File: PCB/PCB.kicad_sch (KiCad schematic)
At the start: 111 parts, among them J1 USB_B_Micro, J2 Conn_01x02, Q1 PJA3428, Q2 PJA3428, Q3 AO3401A, SW1 SW_Push, SW2 SW_Push, SW3 SW_Push, SW4 ON/OFF, U1 ESP32-PICO-MINI-02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

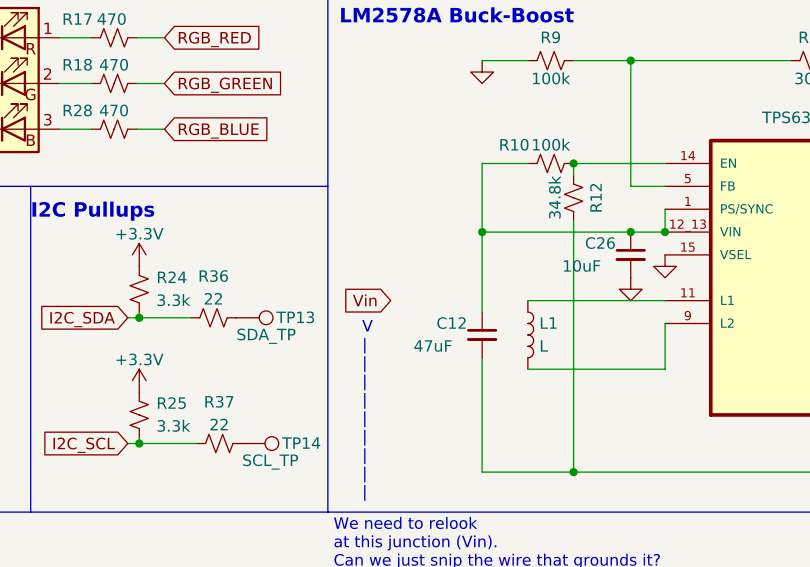
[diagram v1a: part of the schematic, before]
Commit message: buck-boost edits
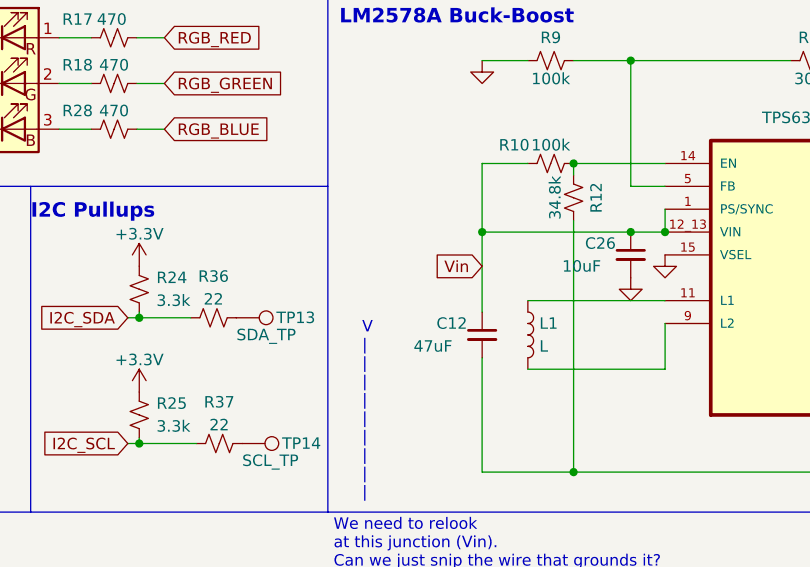
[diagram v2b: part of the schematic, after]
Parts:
- L1: footprint Inductor_SMD:L_0805_2012Metric_Pad1.15x1.40mm_HandSolder -> inductor:IHLP1212BZERR56M11
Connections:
- net Vin: now also C12.1, C26.1, R10.1, U4.1 (PS/SYNC), U4.12_13 (VIN)
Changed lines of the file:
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@@
     )
   )
-  (global_label "Vin" (shape input) (at 295.91 124.46 180) (fields_autoplaced)
+  (global_label "Vin" (shape input) (at 306.07 120.65 180) (fields_autoplaced)
     (effects (font (size 1.27 1.27)) (justify right))
-    (property "Intersheet References" "${INTERSHEET_REFS}" (id 0) (at 290.6545 124.3806 0)
+    (property "Intersheet References" "${INTERSHEET_REFS}" (id 0) (at 300.8145 120.5706 0)
       (effects (font (size 1.27 1.27)) (justify right) hide)
     )
@@
       (effects (font (size 1.27 1.27)) (justify left))
     )
-    (property "Footprint" "Inductor_SMD:L_0805_2012Metric_Pad1.15x1.40mm_HandSolder" (id 2) (at 311.15 128.27 0)
+    (property "Footprint" "inductor:IHLP1212BZERR56M11" (id 2) (at 311.15 128.27 0)
       (effects (font (size 1.27 1.27)) hide)
     )
@@
     )
     (path "/c386aa6a-54a9-4a0e-9ad5-3e2e9aeae025"
-      (reference "L1") (unit 1) (value "L") (footprint "Inductor_SMD:L_0805_2012Metric_Pad1.15x1.40mm_HandSolder")
+      (reference "L1") (unit 1) (value "L") (footprint "inductor:IHLP1212BZERR56M11")
     )
     (path "/cef27ab4-b73f-410e-8967-9f4b41c610a5"

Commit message: buck-boost routing 1
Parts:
- C12: footprint Capacitor_SMD:C_0603_1608Metric -> Capacitor_SMD:C_1206_3216Metric_Pad1.33x1.80mm_HandSolder
- C13: footprint Capacitor_SMD:C_0603_1608Metric -> Capacitor_SMD:C_0402_1005Metric_Pad0.74x0.62mm_HandSolder
- C14: footprint Capacitor_SMD:C_0603_1608Metric -> Capacitor_SMD:C_0201_0603Metric
- C17: footprint Capacitor_SMD:C_0603_1608Metric -> Capacitor_SMD:C_1206_3216Metric
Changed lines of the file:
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@@
       (effects (font (size 1.27 1.27)) (justify left))
     )
-    (property "Footprint" "Capacitor_SMD:C_0603_1608Metric" (id 2) (at 367.03 125.73 0)
+    (property "Footprint" "Capacitor_SMD:C_0402_1005Metric_Pad0.74x0.62mm_HandSolder" (id 2) (at 367.03 125.73 0)
       (effects (font (size 1.27 1.27)) hide)
     )
@@
       (effects (font (size 1.27 1.27)) (justify left))
     )
-    (property "Footprint" "Capacitor_SMD:C_0603_1608Metric" (id 2) (at 389.89 124.46 0)
+    (property "Footprint" "Capacitor_SMD:C_0201_0603Metric" (id 2) (at 389.89 124.46 0)
       (effects (font (size 1.27 1.27)) hide)
     )
@@
       (effects (font (size 1.27 1.27)) (justify left))
     )
-    (property "Footprint" "Capacitor_SMD:C_0603_1608Metric" (id 2) (at 306.07 128.27 0)
+    (property "Footprint" "Capacitor_SMD:C_1206_3216Metric_Pad1.33x1.80mm_HandSolder" (id 2) (at 306.07 128.27 0)
       (effects (font (size 1.27 1.27)) hide)
     )
@@
       (effects (font (size 1.27 1.27)) (justify left))
     )
-    (property "Footprint" "Capacitor_SMD:C_0603_1608Metric" (id 2) (at 397.51 124.46 0)
+    (property "Footprint" "Capacitor_SMD:C_1206_3216Metric" (id 2) (at 397.51 124.46 0)
       (effects (font (size 1.27 1.27)) hide)
     )
@@
     )
     (path "/395ec407-9028-49e9-8808-58f5d58d2657"
-      (reference "C12") (unit 1) (value "47uF") (footprint "Capacitor_SMD:C_0603_1608Metric")
+      (reference "C12") (unit 1) (value "47uF") (footprint "Capacitor_SMD:C_1206_3216Metric_Pad1.33x1.80mm_HandSolder")
     )
     (path "/1064231c-bfd3-489f-ae80-b5249537604d"
-      (reference "C13") (unit 1) (value "10uF") (footprint "Capacitor_SMD:C_0603_1608Metric")
+      (reference "C13") (unit 1) (value "10uF") (footprint "Capacitor_SMD:C_0402_1005Metric_Pad0.74x0.62mm_HandSolder")
     )
     (path "/1efd981a-b294-4f8f-8a3b-cd723ec3f3c5"
-      (reference "C14") (unit 1) (value "10uF") (footprint "Capacitor_SMD:C_0603_1608Metric")
+      (reference "C14") (unit 1) (value "10uF") (footprint "Capacitor_SMD:C_0201_0603Metric")
     )
     (path "/5cf5aff0-dc8a-4f55-b7fe-2729fa1be8c6"
@@
     )
     (path "/62c4ea4f-a8d4-412b-b281-d9bb9978b21a"
-      (reference "C17") (unit 1) (value "47uF") (footprint "Capacitor_SMD:C_0603_1608Metric")
+      (reference "C17") (unit 1) (value "47uF") (footprint "Capacitor_SMD:C_1206_3216Metric")
     )
     (path "/d95f2a14-12b0-408b-b3aa-ddfd14eabcf1"

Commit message: buck/boost
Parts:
- C13: footprint Capacitor_SMD:C_0402_1005Metric_Pad0.74x0.62mm_HandSolder -> Capacitor_SMD:C_0603_1608Metric
- C14: footprint Capacitor_SMD:C_0201_0603Metric -> Capacitor_SMD:C_0603_1608Metric
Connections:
- net +3.3V: now also C14.1, C17.1, C27.1, R13.1, R14.1, U4.7_8 (VOUT)
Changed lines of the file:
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@@
   (junction (at 326.39 116.84) (diameter 0) (color 0 0 0 0)
   )
+  (junction (at 397.51 121.92) (diameter 0) (color 0 0 0 0)
+  )
   (junction (at 375.285 33.02) (diameter 0) (color 0 0 0 0)
   )
@@
       (effects (font (size 1.27 1.27)) (justify left))
     )
-    (property "Footprint" "Capacitor_SMD:C_0402_1005Metric_Pad0.74x0.62mm_HandSolder" (id 2) (at 367.03 125.73 0)
+    (property "Footprint" "Capacitor_SMD:C_0603_1608Metric" (id 2) (at 367.03 125.73 0)
       (effects (font (size 1.27 1.27)) hide)
     )
@@
       (effects (font (size 1.27 1.27)) (justify left))
     )
-    (property "Footprint" "Capacitor_SMD:C_0201_0603Metric" (id 2) (at 389.89 124.46 0)
+    (property "Footprint" "Capacitor_SMD:C_0603_1608Metric" (id 2) (at 389.89 124.46 0)
       (effects (font (size 1.27 1.27)) hide)
     )
@@
     (pin "2")
   )
+  (symbol (lib_id "power:+3.3V") (at 397.51 121.92 0) (unit 1)
+    (in_bom yes) (on_board yes)
+    (property "Reference" "#PWR?" (id 0) (at 397.51 125.73 0)
+      (effects (font (size 1.27 1.27)) hide)
+    )
+    (property "Value" "+3.3V" (id 1) (at 397.51 118.11 0))
+    (property "Footprint" "" (id 2) (at 397.51 121.92 0)
+      (effects (font (size 1.27 1.27)) hide)
+    )
+    (property "Datasheet" "" (id 3) (at 397.51 121.92 0)
+      (effects (font (size 1.27 1.27)) hide)
+    )
+    (pin "1")
+  )
   (symbol (lib_id "power:+3.3V") (at 16.51 67.945 0) (unit 1)
     (in_bom yes) (on_board yes) (fields_autoplaced)
@@
       (reference "#PWR0133") (unit 1) (value "GND") (footprint "")
     )
+    (path "/f9a82e16-6e31-40b7-8380-a1ae7b429d70"
+      (reference "#PWR?") (unit 1) (value "+3.3V") (footprint "")
+    )
     (path "/52cf2d49-7911-4779-ac42-2bcd30f30395"
       (reference "C1") (unit 1) (value "10uF") (footprint "Capacitor_SMD:C_0603_1608Metric")
@@
     )
     (path "/1064231c-bfd3-489f-ae80-b5249537604d"
-      (reference "C13") (unit 1) (value "10uF") (footprint "Capacitor_SMD:C_0402_1005Metric_Pad0.74x0.62mm_HandSolder")
+      (reference "C13") (unit 1) (value "10uF") (footprint "Capacitor_SMD:C_0603_1608Metric")
     )
     (path "/1efd981a-b294-4f8f-8a3b-cd723ec3f3c5"
-      (reference "C14") (unit 1) (value "10uF") (footprint "Capacitor_SMD:C_0201_0603Metric")
+      (reference "C14") (unit 1) (value "10uF") (footprint "Capacitor_SMD:C_0603_1608Metric")
     )
     (path "/5cf5aff0-dc8a-4f55-b7fe-2729fa1be8c6"

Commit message: buck/boost more progress
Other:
- note added: "TPS63070 Buck-Boost"
- note removed: "LM2578A Buck-Boost"
- note removed: "V | | | | | | | | |"
- note removed: "We need to relook at this junction (Vin). Can we just snip the wire that grounds it?"
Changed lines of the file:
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@@
     (effects (font (size 1.6 1.6) (thickness 0.32) bold) (justify left bottom))
-  )
-  (text "We need to relook \nat this junction (Vin).\nCan we just snip the wire that grounds it?"
-    (at 289.56 154.305 0)
-    (effects (font (size 1.27 1.27)) (justify left bottom))
   )
   (text "ESP32\n" (at 13.335 60.325 0)
@@
     (effects (font (size 1.27 1.27) bold) (justify left bottom))
   )
-  (text "V\n|\n|\n|\n|\n|\n|\n|\n|\n|" (at 292.735 146.685 0)
-    (effects (font (size 1.27 1.27)) (justify left bottom))
-  )
   (text "ESP32 Auto-Program Transistors" (at 13.335 151.765 0)
     (effects (font (size 1.6 1.6) (thickness 0.32) bold) (justify left bottom))
@@
     (effects (font (size 1.6 1.6) (thickness 0.32) bold) (justify left bottom))
   )
-  (text "LM2578A Buck-Boost" (at 290.195 93.98 0)
+  (text "TPS63070 Buck-Boost" (at 288.925 92.075 0)
     (effects (font (size 1.6 1.6) (thickness 0.32) bold) (justify left bottom))
   )

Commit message: button update
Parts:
- removed TP1: TDI, TestPoint:TestPoint_Pad_D1.0mm, symbol Connector:TestPoint
- removed TP10: TDO, TestPoint:TestPoint_Pad_D1.0mm, symbol Connector:TestPoint
- removed TP2: TCK, TestPoint:TestPoint_Pad_D1.0mm, symbol Connector:TestPoint
- removed TP9: TMS, TestPoint:TestPoint_Pad_D1.0mm, symbol Connector:TestPoint
- added C28: 100nF, Capacitor_SMD:C_0603_1608Metric, symbol Device:C_Small
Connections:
- net GND: now also C28.2
- net SESSION_BUTTON: now also C28.1
- no-connect marks 12 -> 16
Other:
- moved on the sheet: R24, R25, R36, R37, R39, R40, R41, R42, TP13, TP14

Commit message: final changes
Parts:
- D2: value 1N4148 -> B5819W
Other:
- moved on the sheet: C28, R21, SW3
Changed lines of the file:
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@@
   (junction (at 321.945 60.96) (diameter 0) (color 0 0 0 0)
   )
-  (junction (at 245.745 129.54) (diameter 0) (color 0 0 0 0)
+  (junction (at 253.365 128.905) (diameter 0) (color 0 0 0 0)
   )
   (junction (at 389.89 143.51) (diameter 0) (color 0 0 0 0)
@@
     (stroke (width 0) (type default) (color 0 0 0 0))
   )
-  (wire (pts (xy 245.745 129.54) (xy 245.745 130.81))
+  (wire (pts (xy 253.365 128.905) (xy 253.365 130.175))
     (stroke (width 0) (type default) (color 0 0 0 0))
   )
@@
     (stroke (width 0) (type default) (color 0 0 0 0))
   )
-  (wire (pts (xy 254.635 133.35) (xy 254.635 129.54))
+  (wire (pts (xy 262.255 132.715) (xy 262.255 128.905))
     (stroke (width 0) (type default) (color 0 0 0 0))
   )
@@
     (stroke (width 0) (type default) (color 0 0 0 0))
   )
-  (wire (pts (xy 245.745 128.905) (xy 245.745 129.54))
+  (wire (pts (xy 253.365 128.27) (xy 253.365 128.905))
     (stroke (width 0) (type default) (color 0 0 0 0))
   )
@@
     (stroke (width 0) (type default) (color 0 0 0 0))
   )
-  (wire (pts (xy 245.11 129.54) (xy 245.745 129.54))
+  (wire (pts (xy 252.73 128.905) (xy 253.365 128.905))
     (stroke (width 0) (type default) (color 0 0 0 0))
   )
@@
     (stroke (width 0) (type default) (color 0 0 0 0))
   )
-  (wire (pts (xy 254.635 129.54) (xy 245.745 129.54))
+  (wire (pts (xy 262.255 128.905) (xy 253.365 128.905))
     (stroke (width 0) (type default) (color 0 0 0 0))
   )
@@
     )
   )
-  (global_label "SESSION_BUTTON" (shape input) (at 245.11 129.54 180) (fields_autoplaced)
+  (global_label "SESSION_BUTTON" (shape input) (at 252.73 128.905 180) (fields_autoplaced)
     (effects (font (size 1.27 1.27)) (justify right))
-    (property "Intersheet References" "${INTERSHEET_REFS}" (id 0) (at 226.4893 129.4606 0)
+    (property "Intersheet References" "${INTERSHEET_REFS}" (id 0) (at 234.1093 128.8256 0)
       (effects (font (size 1.27 1.27)) (justify right) hide)
     )
@@
     (pin "1")
   )
-  (symbol (lib_id "power:GND") (at 245.745 140.97 0) (unit 1)
+  (symbol (lib_id "power:GND") (at 253.365 140.335 0) (unit 1)
     (in_bom yes) (on_board yes)
-    (property "Reference" "#PWR0123" (id 0) (at 245.745 147.32 0)
+    (property "Reference" "#PWR0123" (id 0) (at 253.365 146.685 0)
       (effects (font (size 1.27 1.27)) hide)
     )
-    (property "Value" "GND" (id 1) (at 250.825 144.78 0)
+    (property "Value" "GND" (id 1) (at 258.445 144.145 0)
       (effects (font (size 1.27 1.27)) hide)
     )
-    (property "Footprint" "" (id 2) (at 245.745 140.97 0)
+    (property "Footprint" "" (id 2) (at 253.365 140.335 0)
       (effects (font (size 1.27 1.27)) hide)
     )
-    (property "Datasheet" "" (id 3) (at 245.745 140.97 0)
+    (property "Datasheet" "" (id 3) (at 253.365 140.335 0)
       (effects (font (size 1.27 1.27)) hide)
     )
@@
     (pin "1")
   )
-  (symbol (lib_id "Switch:SW_Push") (at 245.745 135.89 270) (unit 1)
+  (symbol (lib_id "Switch:SW_Push") (at 253.365 135.255 270) (unit 1)
     (in_bom yes) (on_board yes)
-    (property "Reference" "SW3" (id 0) (at 244.475 135.255 90)
+    (property "Reference" "SW3" (id 0) (at 252.095 134.62 90)
       (effects (font (size 1.27 1.27)) (justify right))
     )
-    (property "Value" "SW_Push" (id 1) (at 244.475 137.16 90)
+    (property "Value" "SW_Push" (id 1) (at 252.095 136.525 90)
       (effects (font (size 1.27 1.27)) (justify right))
     )
-    (property "Footprint" "Button_Switch_THT:SW_Tactile_SPST_Angled_PTS645Vx58-2LFS" (id 2) (at 250.825 135.89 0)
+    (property "Footprint" "Button_Switch_THT:SW_Tactile_SPST_Angled_PTS645Vx58-2LFS" (id 2) (at 258.445 135.255 0)
       (effects (font (size 1.27 1.27)) hide)
     )
-    (property "Datasheet" "~" (id 3) (at 250.825 135.89 0)
+    (property "Datasheet" "~" (id 3) (at 258.445 135.255 0)
       (effects (font (size 1.27 1.27)) hide)
     )
@@
     (pin "2")
   )
-  (symbol (lib_id "power:GND") (at 254.635 138.43 0) (unit 1)
+  (symbol (lib_id "power:GND") (at 262.255 137.795 0) (unit 1)
     (in_bom yes) (on_board yes)
-    (property "Reference" "#PWR0135" (id 0) (at 254.635 144.78 0)
+    (property "Reference" "#PWR0135" (id 0) (at 262.255 144.145 0)
       (effects (font (size 1.27 1.27)) hide)
     )
-    (property "Value" "GND" (id 1) (at 259.715 142.24 0)
+    (property "Value" "GND" (id 1) (at 267.335 141.605 0)
       (effects (font (size 1.27 1.27)) hide)
     )
-    (property "Footprint" "" (id 2) (at 254.635 138.43 0)
+    (property "Footprint" "" (id 2) (at 262.255 137.795 0)
       (effects (font (size 1.27 1.27)) hide)
     )
-    (property "Datasheet" "" (id 3) (at 254.635 138.43 0)
+    (property "Datasheet" "" (id 3) (at 262.255 137.795 0)
       (effects (font (size 1.27 1.27)) hide)
     )
@@
   (symbol (lib_id "Diode:1N4148") (at 125.73 30.48 90) (unit 1)
     (in_bom yes) (on_board yes) (fields_autoplaced)
-    (property "Reference" "D2" (id 0) (at 127.762 29.6453 90)
+    (property "Reference" "D2" (id 0) (at 128.27 29.2099 90)
       (effects (font (size 1.27 1.27)) (justify right))
     )
-    (property "Value" "1N4148" (id 1) (at 127.762 32.1822 90)
+    (property "Value" "B5819W" (id 1) (at 128.27 31.7499 90)
       (effects (font (size 1.27 1.27)) (justify right))
     )
@@
     (pin "2")
   )
-  (symbol (lib_id "power:+3.3V") (at 245.745 123.825 0) (unit 1)
+  (symbol (lib_id "power:+3.3V") (at 253.365 123.19 0) (unit 1)
     (in_bom yes) (on_board yes) (fields_autoplaced)
-    (property "Reference" "#PWR0124" (id 0) (at 245.745 127.635 0)
+    (property "Reference" "#PWR0124" (id 0) (at 253.365 127 0)
       (effects (font (size 1.27 1.27)) hide)
     )
-    (property "Value" "+3.3V" (id 1) (at 245.745 120.2492 0))
-    (property "Footprint" "" (id 2) (at 245.745 123.825 0)
+    (property "Value" "+3.3V" (id 1) (at 253.365 119.6142 0))
+    (property "Footprint" "" (id 2) (at 253.365 123.19 0)
       (effects (font (size 1.27 1.27)) hide)
     )
-    (property "Datasheet" "" (id 3) (at 245.745 123.825 0)
+    (property "Datasheet" "" (id 3) (at 253.365 123.19 0)
       (effects (font (size 1.27 1.27)) hide)
     )
@@
     (pin "3")
   )
-  (symbol (lib_id "Device:R_Small_US") (at 245.745 126.365 0) (unit 1)
+  (symbol (lib_id "Device:R_Small_US") (at 253.365 125.73 0) (unit 1)
     (in_bom yes) (on_board yes) (fields_autoplaced)
-    (property "Reference" "R21" (id 0) (at 248.285 125.0949 0)
+    (property "Reference" "R21" (id 0) (at 255.905 124.4599 0)
       (effects (font (size 1.27 1.27)) (justify left))
     )
-    (property "Value" "10k" (id 1) (at 248.285 127.6349 0)
+    (property "Value" "10k" (id 1) (at 255.905 126.9999 0)
       (effects (font (size 1.27 1.27)) (justify left))
     )
-    (property "Footprint" "Resistor_SMD:R_0603_1608Metric" (id 2) (at 245.745 126.365 0)
+    (property "Footprint" "Resistor_SMD:R_0603_1608Metric" (id 2) (at 253.365 125.73 0)
       (effects (font (size 1.27 1.27)) hide)
     )
-    (property "Datasheet" "~" (id 3) (at 245.745 126.365 0)
+    (property "Datasheet" "~" (id 3) (at 253.365 125.73 0)
       (effects (font (size 1.27 1.27)) hide)
     )
@@
     (pin "1")
   )
-  (symbol (lib_id "Device:C_Small") (at 254.635 135.89 0) (unit 1)
+  (symbol (lib_id "Device:C_Small") (at 262.255 135.255 0) (unit 1)
     (in_bom yes) (on_board yes) (fields_autoplaced)
-    (property "Reference" "C28" (id 0) (at 257.175 134.6262 0)
+    (property "Reference" "C28" (id 0) (at 264.795 133.9912 0)
       (effects (font (size 1.27 1.27)) (justify left))
     )
-    (property "Value" "100nF" (id 1) (at 257.175 137.1662 0)
+    (property "Value" "100nF" (id 1) (at 264.795 136.5312 0)
       (effects (font (size 1.27 1.27)) (justify left))
     )
-    (property "Footprint" "Capacitor_SMD:C_0603_1608Metric" (id 2) (at 254.635 135.89 0)
+    (property "Footprint" "Capacitor_SMD:C_0603_1608Metric" (id 2) (at 262.255 135.255 0)
       (effects (font (size 1.27 1.27)) hide)
     )
-    (property "Datasheet" "~" (id 3) (at 254.635 135.89 0)
+    (property "Datasheet" "~" (id 3) (at 262.255 135.255 0)
       (effects (font (size 1.27 1.27)) hide)
     )
@@
     )
     (path "/581ca598-1d01-4057-bec3-5cf6c2d6dd7c"
-      (reference "D2") (unit 1) (value "1N4148") (footprint "Diode_SMD:D_1206_3216Metric")
+      (reference "D2") (unit 1) (value "B5819W") (footprint "Diode_SMD:D_1206_3216Metric")
     )
     (path "/0468a543-7392-406e-a1e2-1b00bf8a5b37"

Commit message: schem edits
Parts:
- C13: value 10uF -> 100 nF
- C27: value 100nF -> 10uF
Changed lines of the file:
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@@
       (effects (font (size 1.27 1.27)) (justify left))
     )
-    (property "Value" "10uF" (id 1) (at 359.41 127 0)
+    (property "Value" "100 nF" (id 1) (at 359.41 127 0)
       (effects (font (size 1.27 1.27)) (justify left))
     )
@@
       (effects (font (size 1.27 1.27)) (justify left))
     )
-    (property "Value" "100nF" (id 1) (at 356.87 120.65 0)
+    (property "Value" "10uF" (id 1) (at 356.87 120.65 0)
       (effects (font (size 1.27 1.27)) (justify left))
     )
@@
     )
     (path "/1064231c-bfd3-489f-ae80-b5249537604d"
-      (reference "C13") (unit 1) (value "10uF") (footprint "Capacitor_SMD:C_0603_1608Metric")
+      (reference "C13") (unit 1) (value "100 nF") (footprint "Capacitor_SMD:C_0603_1608Metric")
     )
     (path "/1efd981a-b294-4f8f-8a3b-cd723ec3f3c5"
@@
     )
     (path "/c2952636-7ad4-4c20-8de3-ed7e9fecf3f5"
-      (reference "C27") (unit 1) (value "100nF") (footprint "Capacitor_SMD:C_0603_1608Metric")
+      (reference "C27") (unit 1) (value "10uF") (footprint "Capacitor_SMD:C_0603_1608Metric")
     )
     (path "/d3bb0cec-8971-4b1a-a87c-b6e52ecd32b6"
